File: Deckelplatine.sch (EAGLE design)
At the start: 57 parts, among them IC1 MAX481CSA, IC2 74HCT595D, IC3 74HCT595D, IC4 74HCT595D, IC5 74HCT595D, IC6 74HCT595D, J1 CON25, U1 LM2676S, X1 ''

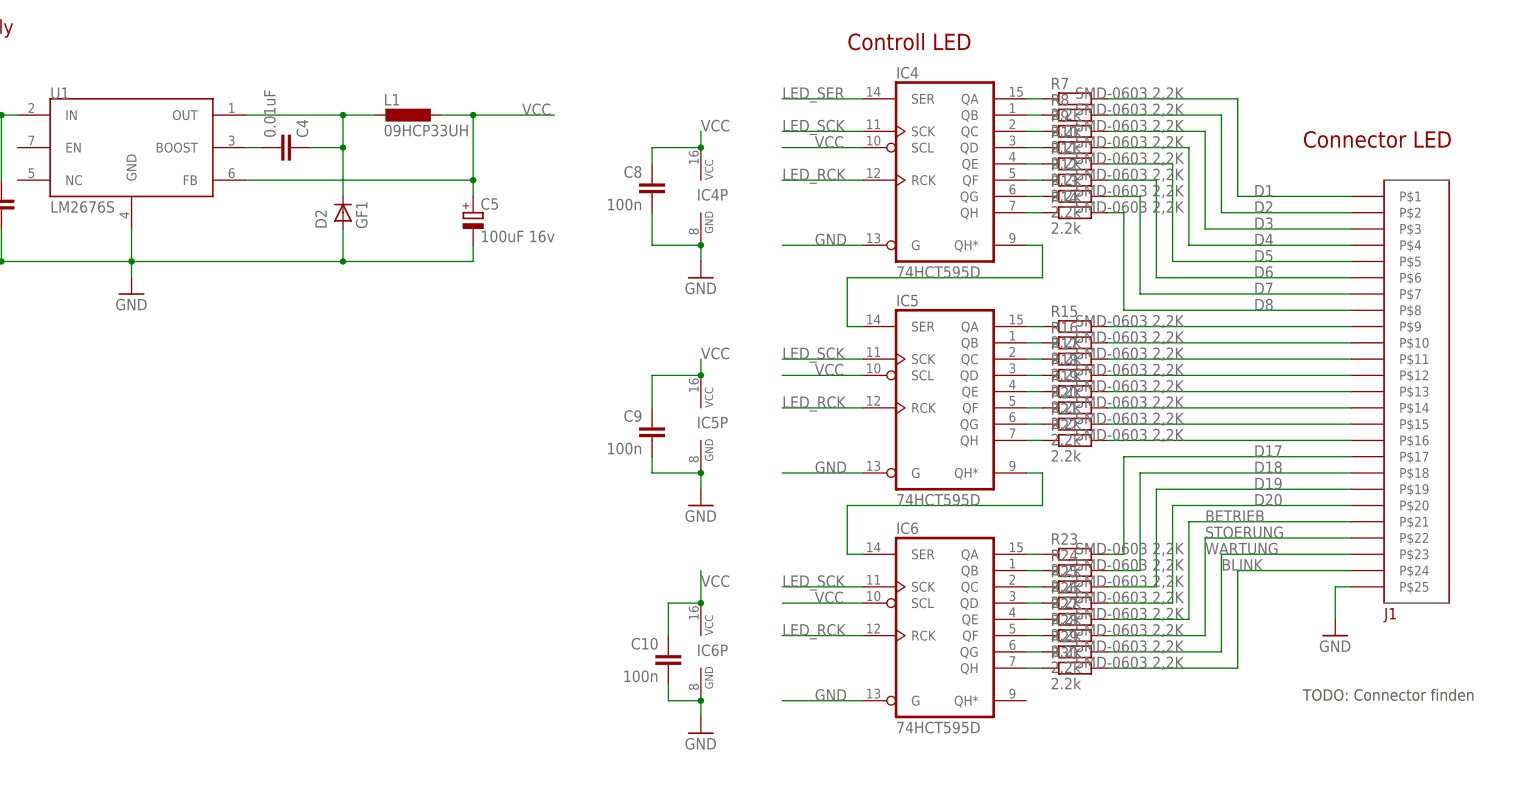
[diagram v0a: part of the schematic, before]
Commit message: Begin mit dem Board Layout
Erste Lieferung von Farnell angekommen.
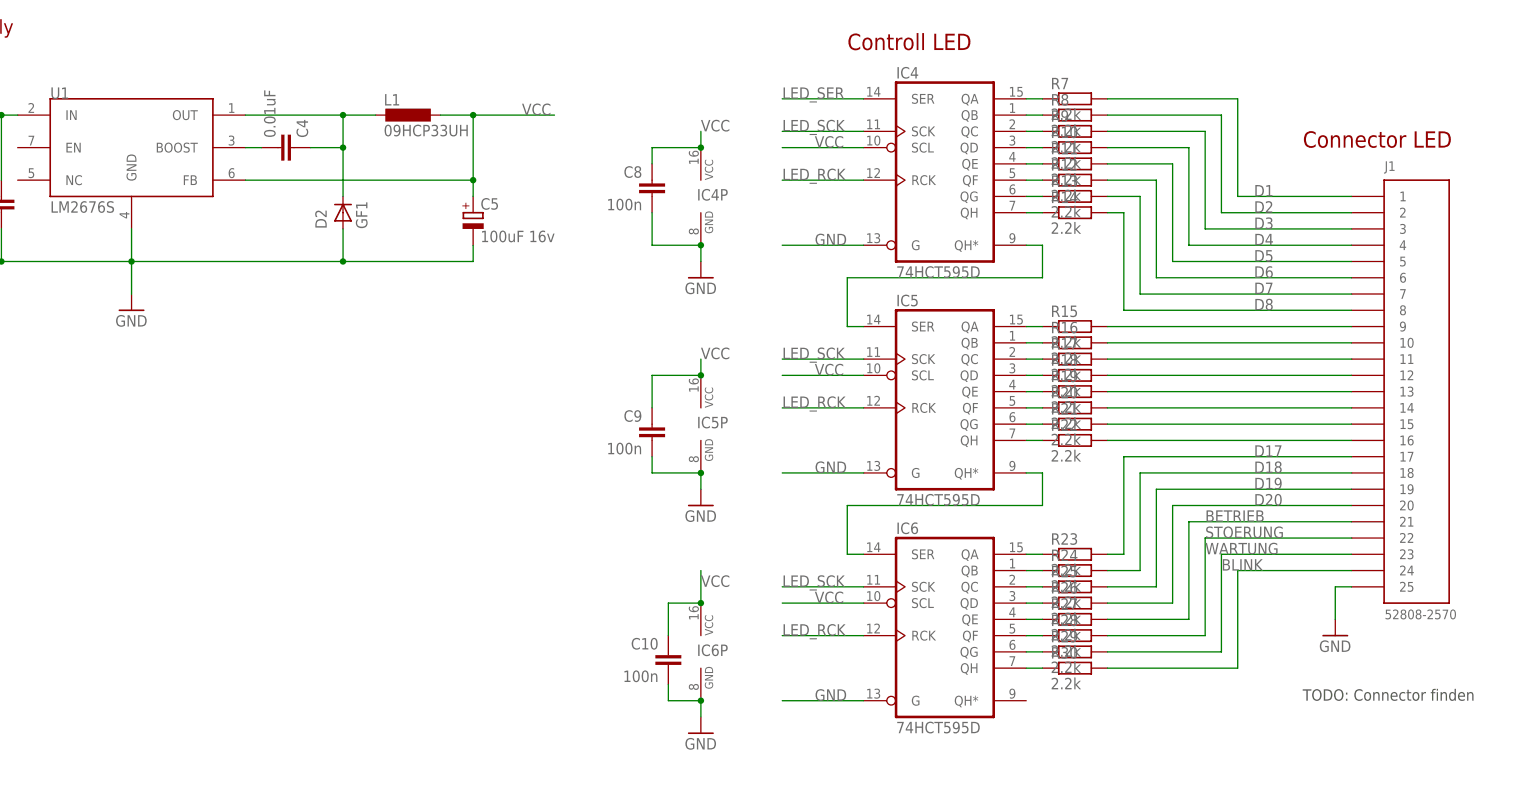
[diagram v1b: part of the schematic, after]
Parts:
- F1: MF SCHURTER -> (none); MPN 3101.0040 -> (none); OC_FARNELL 1222690 -> (none)
- J1: value CON25 -> 52808-2570; device RA-GAS Projekte LTD:CON25 -> RA-GAS Projekte LTD:52808-2570; DNP T -> (none); MF MOLEX -> (none); MPN 52808-2570 -> (none); OC_FARNELL 1757123 -> (none)
- R5: MF VISHAY DRALORIC -> (none); MPN AC03000001500JAC00 -> (none); OC_FARNELL 1735096 -> (none)
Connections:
- net BETRIEB: now also J1.21; no longer J1.P$21
- net BLINK: now also J1.24; no longer J1.P$24
- net D1: now also J1.1; no longer J1.P$1
- net D17: now also J1.17; no longer J1.P$17
- net D18: now also J1.18; no longer J1.P$18
- net D19: now also J1.19; no longer J1.P$19
- net D2: now also J1.2; no longer J1.P$2
- net D20: now also J1.20; no longer J1.P$20
- net D3: now also J1.3; no longer J1.P$3
- net D4: now also J1.4; no longer J1.P$4
- net D5: now also J1.5; no longer J1.P$5
- net D6: now also J1.6; no longer J1.P$6
- net D7: now also J1.7; no longer J1.P$7
- net D8: now also J1.8; no longer J1.P$8
- net GND: now also J1.25; no longer J1.P$25
- net N$31: now also J1.9; no longer J1.P$9
- net N$32: now also J1.10; no longer J1.P$10
- net N$33: now also J1.11; no longer J1.P$11
- net N$34: now also J1.12; no longer J1.P$12
- net N$35: now also J1.13; no longer J1.P$13
- net N$36: now also J1.14; no longer J1.P$14
- net N$37: now also J1.15; no longer J1.P$15
- net N$38: now also J1.16; no longer J1.P$16
- net STOERUNG: now also J1.22; no longer J1.P$22
- net WARTUNG: now also J1.23; no longer J1.P$23

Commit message: Stromlaufplan fast fertig.
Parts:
- added X2: 233-502, con-wago_233:233-502
- C1, C10, C7, C8, C9: device rcl:C-EUC1206 -> resistor:C-EUC0603; MF MULTICOMP -> KEMET; MPN MCCTA104M035 -> C0603C104K8RACTU; OC_FARNELL 1190132 -> 2112833
- C11: value 0.1uF -> 100n; device rcl:C-EUC1206 -> resistor:C-EUC0603; MPN T495X475M050ATE300 -> C0603C104K8RACTU; OC_FARNELL 1692407 -> 2112833; PARTNO X7R-G1210 4,7 -> SMD TAN.0,1/35
- C4: value 0.01uF -> 0.1uF; device rcl:C-EUC0805 -> rcl:C-EUC1206; MF AVX -> KEMET; MPN 0402YC103KAT2A -> T495X475M050ATE300; OC_FARNELL 1327662 -> 1692407; PARTNO X7R-G0805 10N -> X7R-G1210 4,7
- C5: value 100uF 16v -> 0.01uF; device rcl:CPOL-EUD -> rcl:C-EUC0805; MF PANASONIC ELECTRONIC COMPONENTS -> AVX; MPN EEEFT1V561AP -> 0402YC103KAT2A; OC_FARNELL 1868420 -> 1327662; PARTNO RAD FC 560/35 -> X7R-G0805 10N
- C6: value 100n -> 100uF 16v; device rcl:C-EUC1206 -> rcl:CPOL-EUD; MF MULTICOMP -> PANASONIC ELECTRONIC COMPONENTS; MPN MCCTA104M035 -> EEEFT1V561AP; OC_FARNELL 1190132 -> 1868420; PARTNO SMD TAN.0,1/35 -> RAD FC 560/35
- F1: device fuse:KS9V -> fuse-schurter:FPG4-3101.0040; MF (none) -> SCHURTER; MPN (none) -> 3101.0040; OC_FARNELL (none) -> 1222690
- IC1: value MAX481CSA -> MAX1487EESA+; MPN MAX481CSA+ -> MAX1487EESA+; OC_FARNELL 2113664 -> 1593310
- J1: MF (none) -> MOLEX; MPN (none) -> 52808-2570; OC_FARNELL (none) -> 1757123
- JP1: value CON6 -> ''
- JP2: MPN 1-825433-0 -> 825433-2; OC_FARNELL 1187829 -> 3417645
- L1: value 09HCP33UH -> DO5022P-EU_; device Inductor-Fastron:09HCP33UH -> RA-GAS Projekte LTD:DO5022P-EU_
- X1: value '' -> 236-404; device con-wago:233-504 -> con-wago_236:236-404; MPN 233-504. -> 236-404; OC_FARNELL (none) -> 1283528; PARTNO WAGO 233-504 -> (none)
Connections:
- net BETRIEB renamed D21
- net BLINK renamed D24
- net N$31 renamed D9
- net N$32 renamed D10
- net N$33 renamed D11
- net N$34 renamed D12
- net N$35 renamed D13
- net N$36 renamed D14
- net N$37 renamed D15
- net N$38 renamed D16
- net STOERUNG renamed D22
- net WARTUNG renamed D23
- new net N$31: F1.2, F1.2@2
- net 12V_VIN: now also C4.1, X1.P1.1, X1.P1.2; no longer C11.1, X1.B-1
- net ACCU+: now also F1.1@1, X1.P3.1, X1.P3.2; no longer X1.B-3
- net ACCU-: now also X1.P4.1, X1.P4.2; no longer X1.B-4
- net GND: now also C4.2, C6.-, X1.P2.1, X1.P2.2, X2.P2.1, X2.P2.2; no longer C5.-, C6.2, X1.B-2
- net N$1: no longer F1.2
- net N$42: now also C5.2; no longer C4.2
- net N$44: now also C5.1, L1.1; no longer C4.1, L1.2
- net VCC: now also C11.1, C6.+, L1.2, X2.P1.1, X2.P1.2; no longer C5.+, C6.1, L1.1
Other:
- note added: "Connector Banana Pro Power SATA"
- moved on the sheet: C1, C10, C11, C2, C3, C4, C7, C8, C9, IC1, IC1P, IC2P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

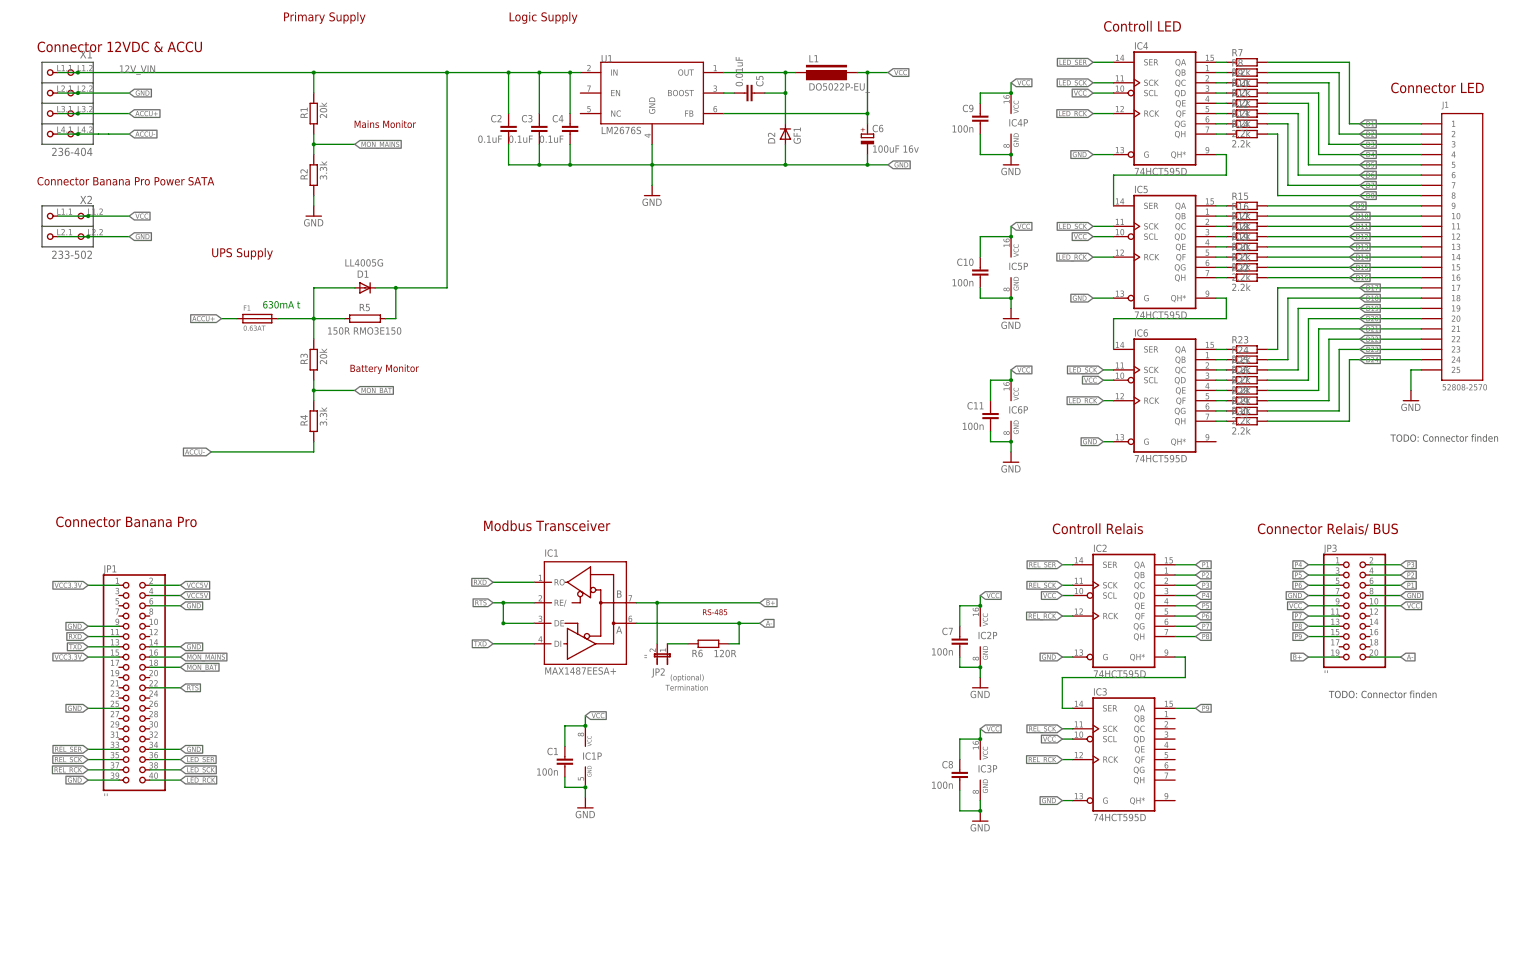
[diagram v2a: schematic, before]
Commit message: Schema mit Verpolschutz an Vin und Accu.
Schaltregler nach Application Note von Texas Instruments.
Eingänge für den MON_MAINS und MON_BAT (GPIO Banana Pro Eingänge zur Überwachung Vin und Accu) sind durch NPN Transistoren gegen Überspannunge geschützt
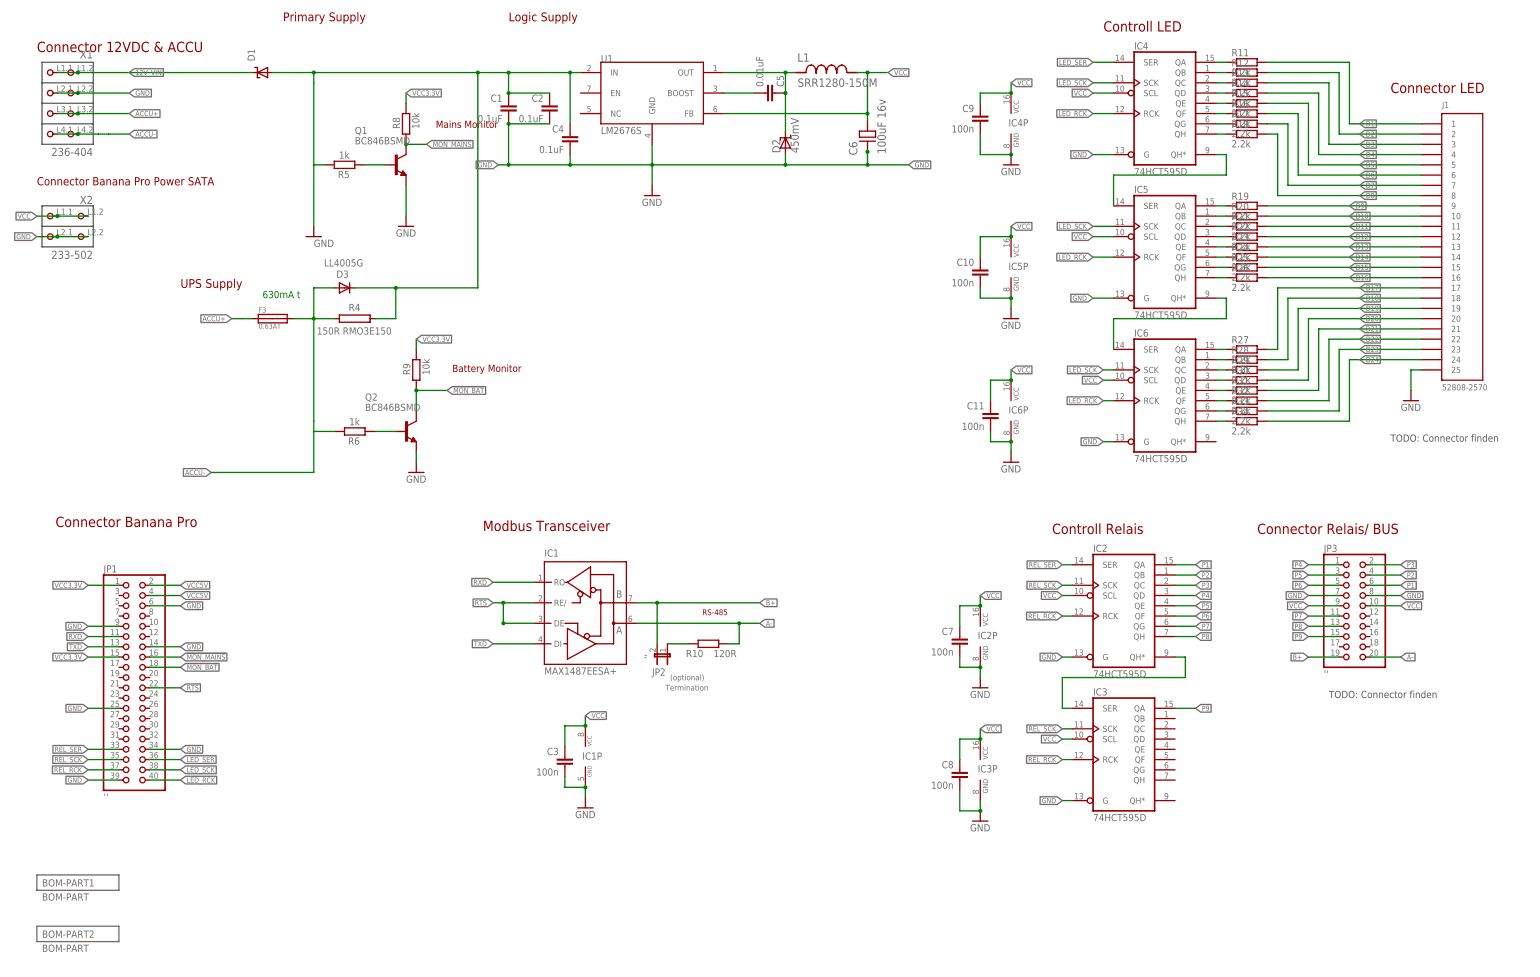
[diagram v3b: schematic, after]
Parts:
- removed F1: 0.63AT, fuse-schurter:FPG4-3101.0040
- removed R1, R3: 20k, rcl:R-EU_R1206
- removed R2: 3.3k, rcl:R-EU_R1206
- removed R7: 2.2k, RA-GAS Projekte LTD:R-EU_R0603
- added D3: LL4005G, diode:DIODE-MELF-MLL41
- added F3: 0.63AT, fuse-schurter:FPG4-3101.0040
- added Q1, Q2: BC846BSMD, transistor-npn:BC846BSMD
- added R31, R32, R33, R34: 2.2k, RA-GAS Projekte LTD:R-EU_R0603
- C1: value 100n -> 0.1uF; device resistor:C-EUC0603 -> AcceleratedDesigns_Lib:GRM21BR61E475MA12L; MPN C0603C104K8RACTU -> T495X475M050ATE300; OC_FARNELL 2112833 -> 1692407; PARTNO ECHU-16-100N -> X7R-G1210 4,7
- C2: device rcl:C-EUC1206 -> AcceleratedDesigns_Lib:GRM21BR61E475MA12L
- C3: value 0.1uF -> 100n; device rcl:C-EUC1206 -> resistor:C-EUC0603; MPN T495X475M050ATE300 -> C0603C104K8RACTU; OC_FARNELL 1692407 -> 2112833; PARTNO X7R-G1210 4,7 -> ECHU-16-100N
- C4: device rcl:C-EUC1206 -> AcceleratedDesigns_Lib:08053C104KAT2A
- C5: device rcl:C-EUC0805 -> AcceleratedDesigns_Lib:GRM216R71H103KA01D
- C6: device rcl:CPOL-EUD -> AcceleratedDesigns_Lib:16SVP180M
- D1: value LL4005G -> (none); device diode:DIODE-MELF-MLL41 -> diode:SUPPRESSOR-SMBJ; MF TAIWAN SEMICONDUCTOR -> VISHAY; MPN LL4005G -> SSB44-E3/52T; OC_FARNELL 1625106 -> 1336557; PARTNO 1N 4005 -> (none)
- D2: value GF1 -> 450mV; device diode:GF1 -> AcceleratedDesigns_Lib:B340LB-13-F; MF FAIRCHILD SEMICONDUCTOR -> DIODES INC.; MPN SB360 -> B340LB-13-F; OC_FARNELL 1700739 -> 1843684; PARTNO SB 360 -> (none)
- L1: value DO5022P-EU_ -> SRR1280-150M; device RA-GAS Projekte LTD:DO5022P-EU_ -> AcceleratedDesigns_Lib:SRR1280-150M
- R10: value 2.2k -> 120R; device RA-GAS Projekte LTD:R-EU_R0603 -> rcl:R-EU_R1206; MF YAGEO (PHYCOMP) -> TE CONNECTIVITY; MPN RC0603FR-072K2L -> CRGH1206F120R; OC_FARNELL 9238522 -> 2332128; PARTNO SMD-0603 2,2K -> (none)
- R4: value 3.3k -> 150R RMO3E150; device rcl:R-EU_R1206 -> resistor-power:RKH206-8; MF PANASONIC ELECTRONIC COMPONENTS -> TE CONNECTIVITY / CGS; MPN ERJP14F3301U -> ER74150RJT; OC_FARNELL 1750924 -> 1751842; OC_FARNELL_ALTERNATIVE (none) -> 1735096
- R5: value 150R RMO3E150 -> 1k; device resistor-power:RKH206-8 -> rcl:R-EU_R1210; MF (none) -> PANASONIC ELECTRONIC COMPONENTS; MPN (none) -> ERJP14F1001U; OC_FARNELL (none) -> 1750918
- R6: value 120R -> 1k; device rcl:R-EU_R1206 -> rcl:R-EU_R1210; MF TE CONNECTIVITY -> PANASONIC ELECTRONIC COMPONENTS; MPN CRGH1206F120R -> ERJP14F1001U; OC_FARNELL 2332128 -> 1750918
- R8, R9: value 2.2k -> 10k; device RA-GAS Projekte LTD:R-EU_R0603 -> rcl:R-EU_R1210; MF YAGEO (PHYCOMP) -> PANASONIC ELECTRONIC COMPONENTS; MPN RC0603FR-072K2L -> ERJP14F1002U; OC_FARNELL 9238522 -> 1750931; PARTNO SMD-0603 2,2K -> (none)
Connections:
- removed net MON_BAT: JP1.18, R3.1, R4.2
- removed net MON_MAINS: JP1.16, R1.1, R2.2
- removed net N$1: D1.A, R3.2, R5.1
- removed net N$31: F1.2, F1.2@2
- new net !MON_BAT: JP1.18, Q2.C, R6.2, R9.1
- new net !MON_MAINS: JP1.16, Q1.C, R5.2, R8.1
- new net N$37: Q1.B, R5.1
- new net N$38: D3.A, F3.P$2, R4.1
- new net N$39: F3.P$1
- new net N$4: Q2.B, R6.1
- new net V+: D3.C, R4.2
- net 12V_VIN: now also C1.1, D1.A; no longer C3.1, R1.2, R5.2
- net A-: now also R10.2; no longer R6.2
- net ACCU+: no longer F1.1, F1.1@1
- net ACCU-: no longer R4.1
- net D1: now also R11.2; no longer R7.2
- net D10: now also R20.2; no longer R16.2
- net D11: now also R21.2; no longer R17.2
- net D12: now also R22.2; no longer R18.2
- net D13: now also R23.2; no longer R19.2
- net D14: now also R24.2; no longer R20.2
- net D15: now also R25.2; no longer R21.2
- net D16: now also R26.2; no longer R22.2
- net D17: now also R27.2; no longer R23.2
- net D18: now also R28.2; no longer R24.2
- net D19: now also R29.2; no longer R25.2
- net D2: now also R12.2; no longer R8.2
- net D20: now also R30.2; no longer R26.2
- net D21: now also R31.2; no longer R27.2
- net D22: now also R32.2; no longer R28.2
- net D23: now also R33.2; no longer R29.2
- net D24: now also R34.2; no longer R30.2
- net D3: now also R13.2; no longer R9.2
- net D4: now also R14.2; no longer R10.2
- net D5: now also R15.2; no longer R11.2
- net D6: now also R16.2; no longer R12.2
- net D7: now also R17.2; no longer R13.2
- net D8: now also R18.2; no longer R14.2
- net D9: now also R19.2; no longer R15.2
- net GND: now also Q1.E, Q2.E; no longer R2.1
- net N$10: now also R15.1; no longer R11.1
- net N$11: now also R16.1; no longer R12.1
- net N$12: now also R17.1; no longer R13.1
- net N$13: now also R18.1; no longer R14.1
- net N$14: now also R19.1; no longer R15.1
- net N$15: now also R20.1; no longer R16.1
- net N$16: now also R21.1; no longer R17.1
- net N$17: now also R22.1; no longer R18.1
- net N$18: now also R10.1; no longer R6.1
- net N$19: now also R23.1; no longer R19.1
- net N$20: now also R24.1; no longer R20.1
- net N$21: now also R25.1; no longer R21.1
- net N$22: now also R26.1; no longer R22.1
- net N$23: now also R27.1; no longer R23.1
- net N$24: now also R28.1; no longer R24.1
- net N$25: now also R29.1; no longer R25.1
- net N$26: now also R30.1; no longer R26.1
- net N$27: now also R31.1; no longer R27.1
- net N$28: now also R32.1; no longer R28.1
- net N$29: now also R33.1; no longer R29.1
- net N$30: now also R34.1; no longer R30.1
- net N$44: now also D2.K; no longer D2.C
- net N$6: now also R11.1; no longer R7.1
- net N$7: now also R12.1; no longer R8.1
- net N$8: now also R13.1; no longer R9.1
- net N$9: now also R14.1; no longer R10.1
- net VCC: now also C3.1; no longer C1.1
- net VCC3.3V: now also R8.2, R9.2
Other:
- moved on the sheet: C3, R10, R11, R12, R13, R14, R15, R16, R17, R18, R19, R20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
